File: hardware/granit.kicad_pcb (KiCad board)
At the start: 4 copper layers, 92 x 100 mm, 120 parts, among them IC1 ASM1061, J1 12V Barrel, J2 12V Screw Terminal, J3 RJ45_RB1-125B8G1A, J6 PCM12SMTR, J7 USB_C_Receptacle_USB2.0_14P, J8 BM03B-SRSS-TB, J9 SATA_22pin, Q1 FDS4435BZ, Q2 FDS4435BZ, Q3 FDS4435BZ, Q4 2N7002, Q5 2N7002, Q6 2N7002, SW1 SW_Push, U1 NCP1117-3.3_SOT223, U2 AP64501SP-13, U3 74AHCT1G125, U4 DS3231MZ, U5 USBLC6-2SC6, U6 74AHCT1G32, Y1 25MHz

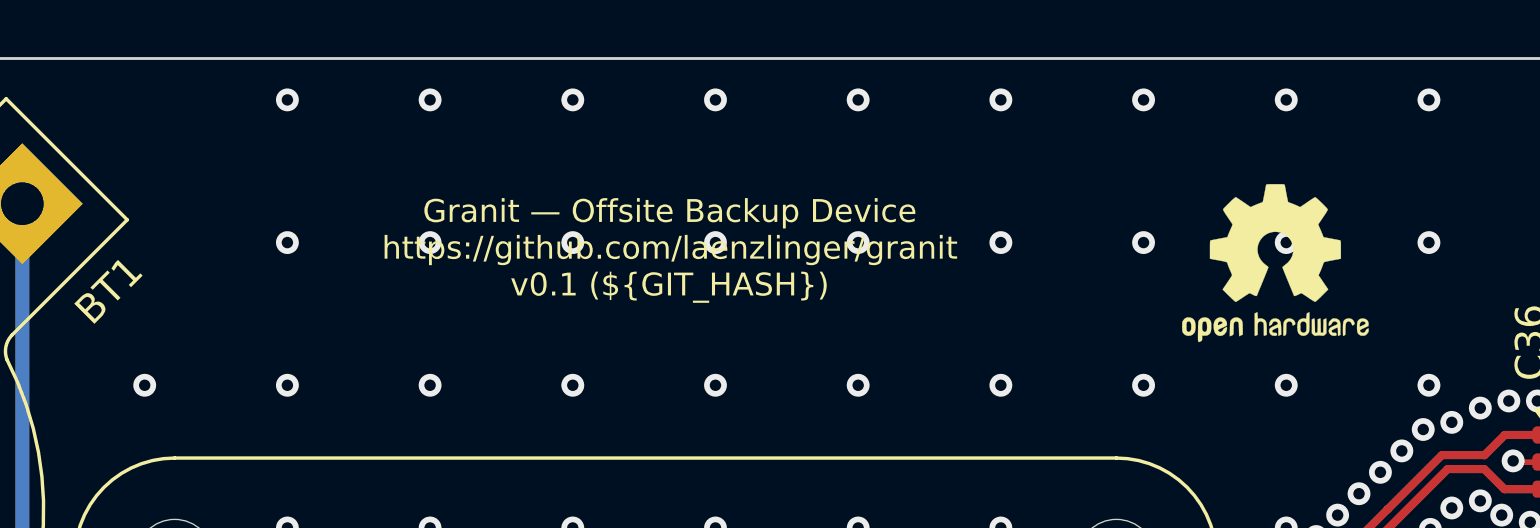
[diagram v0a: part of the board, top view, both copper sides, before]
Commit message: feat: add QR code linking to GitHub repo on front silkscreen
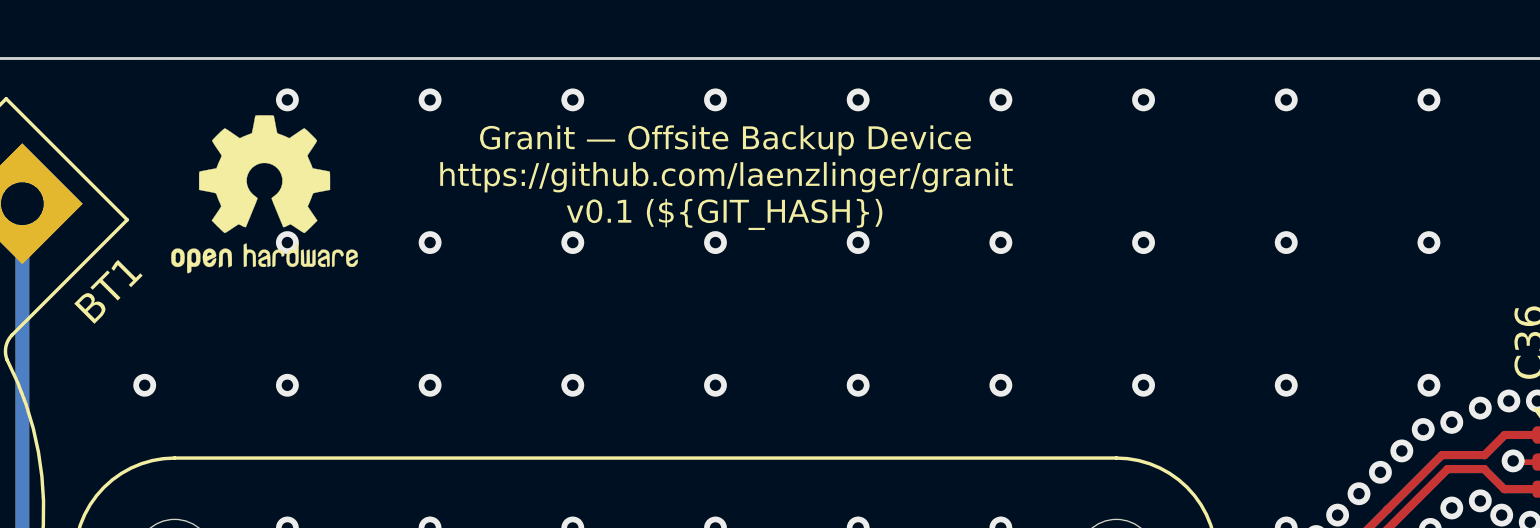
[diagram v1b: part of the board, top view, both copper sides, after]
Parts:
- moved SYM1 35.5 mm to (55.6, 24.8)
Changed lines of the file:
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@@
 	(footprint "Symbol:OSHW-Logo2_7.3x6mm_SilkScreen"
 		(layer "F.Cu")
-		(at 91.070714 27.162714)
+		(at 55.65 24.75)
 		(descr "Open Source Hardware Symbol")
 		(tags "Logo Symbol OSHW")
@@
 	)
 	(gr_text "${TITLE}\n${COMPANY}\nv${REVISION} (${GIT_HASH})"
-		(at 69.85 28.4 0)
+		(at 71.8 25.85 0)
 		(layer "F.SilkS")
 		(effects
@@
 		)
 	)
+	(barcode
+		(at 90.75 26.3 0)
+		(layer "F.SilkS")
+		(size 10 10)
+		(text " https://github.com/laenzlinger/granit")
+		(text_height 1)
+		(type qr)
+		(ecc_level M)
+		(hide yes)
+		(knockout no)
+	)
 	(segment

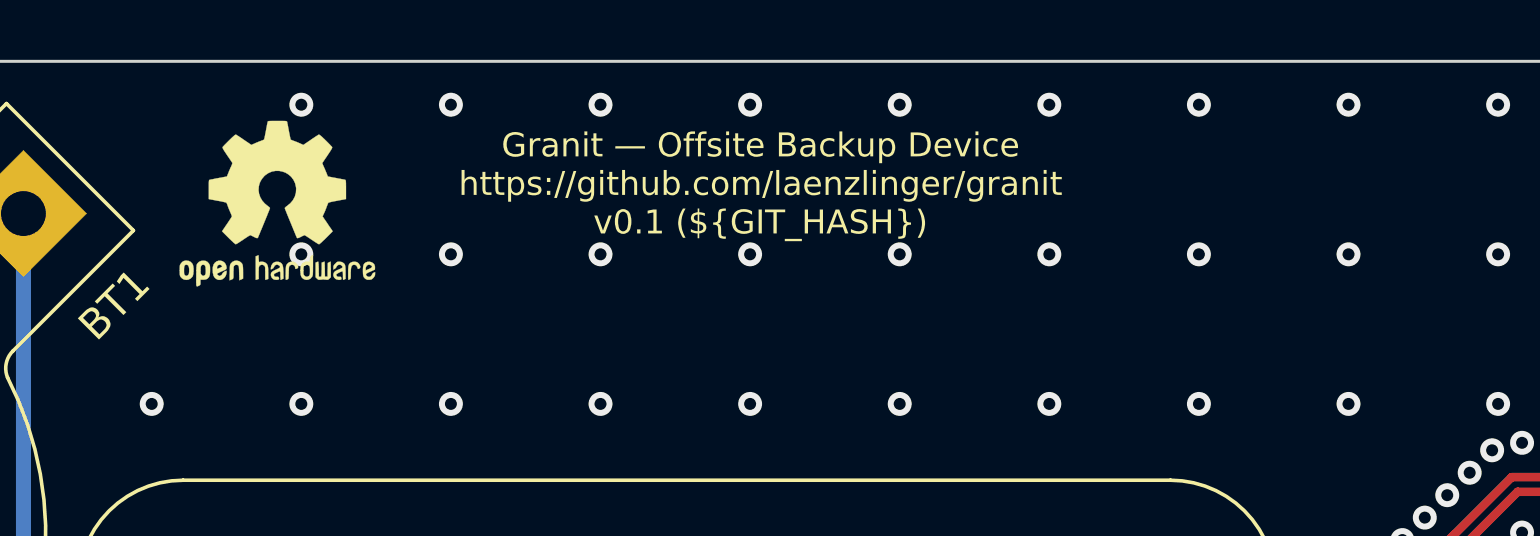
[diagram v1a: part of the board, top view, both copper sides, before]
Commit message: fix: DRC clean — mirror back silkscreen, clear QR code area, re-enable DRC in kibot
ERC: 0 errors, 0 warnings
DRC: 0 violations, 0 unconnected, 0 parity issues
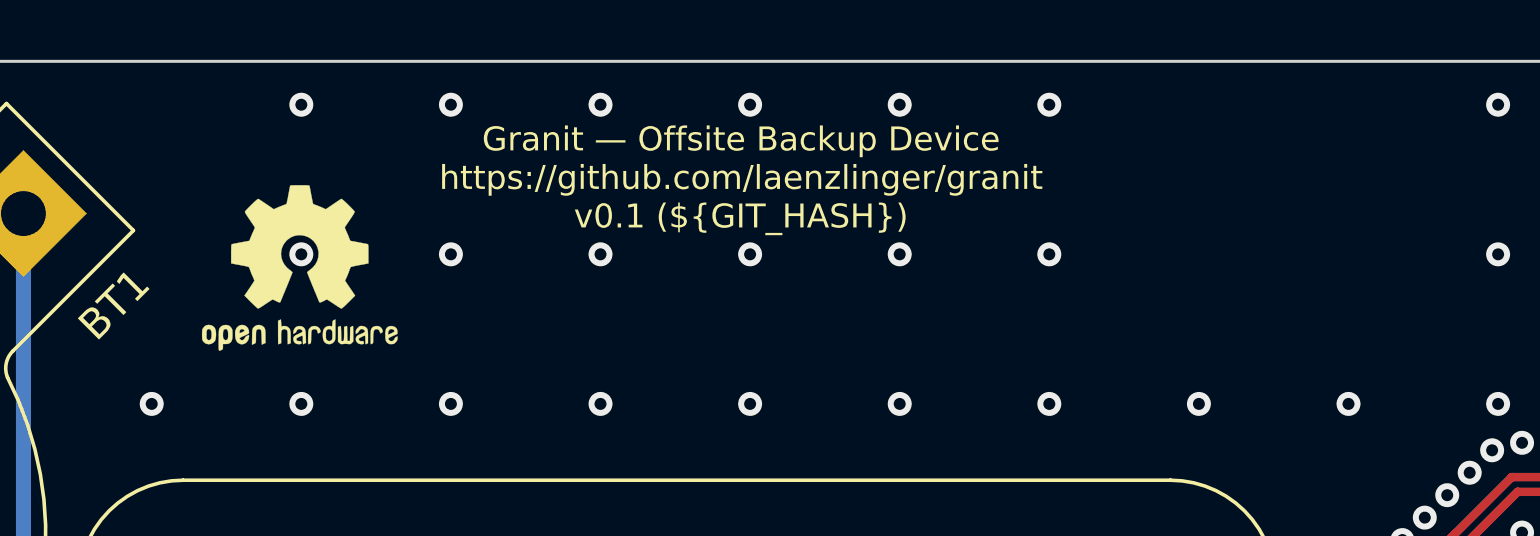
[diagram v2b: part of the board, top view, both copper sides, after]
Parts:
- moved SYM1 2.28 mm to (56.4, 26.9)
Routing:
- net GND: vias 454 -> 450
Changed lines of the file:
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@@
 	(footprint "Symbol:OSHW-Logo2_7.3x6mm_SilkScreen"
 		(layer "F.Cu")
-		(at 55.65 24.75)
+		(at 56.4 26.9)
 		(descr "Open Source Hardware Symbol")
 		(tags "Logo Symbol OSHW")
@@
 	)
 	(gr_text "${TITLE}\n${COMPANY}\nv${REVISION} (${GIT_HASH})"
-		(at 71.8 25.85 0)
+		(at 71.15 25.65 0)
 		(layer "F.SilkS")
 		(effects
@@
 				(thickness 0.15)
 			)
+			(justify mirror)
 		)
 	)
 	(barcode
-		(at 90.75 26.3 0)
+		(at 89.2 25.6 0)
 		(layer "F.SilkS")
-		(size 10 10)
+		(size 9 9)
 		(text " https://github.com/laenzlinger/granit")
 		(text_height 1)
@@
 	)
 	(via
-		(at 86.45 21.45)
-		(size 0.8)
-		(drill 0.4)
-		(layers "F.Cu" "B.Cu")
-		(net "GND")
-	)
-	(via
 		(at 96.5 81.75)
 		(size 0.8)
@@
 	)
 	(via
-		(at 91.45 21.45)
-		(size 0.8)
-		(drill 0.4)
-		(layers "F.Cu" "B.Cu")
-		(net "GND")
-	)
-	(via
 		(at 85.45 116.6)
 		(size 0.8)
@@
 	)
 	(via
-		(at 86.45 26.45)
-		(size 0.8)
-		(drill 0.4)
-		(layers "F.Cu" "B.Cu")
-		(net "GND")
-	)
-	(via
 		(at 44.8 57.25)
 		(size 0.8)
@@
 		(net "GND")
 	)
-	(via
-		(at 91.45 26.45)
-		(size 0.8)
-		(drill 0.4)
-		(layers "F.Cu" "B.Cu")
-		(net "GND")
-	)

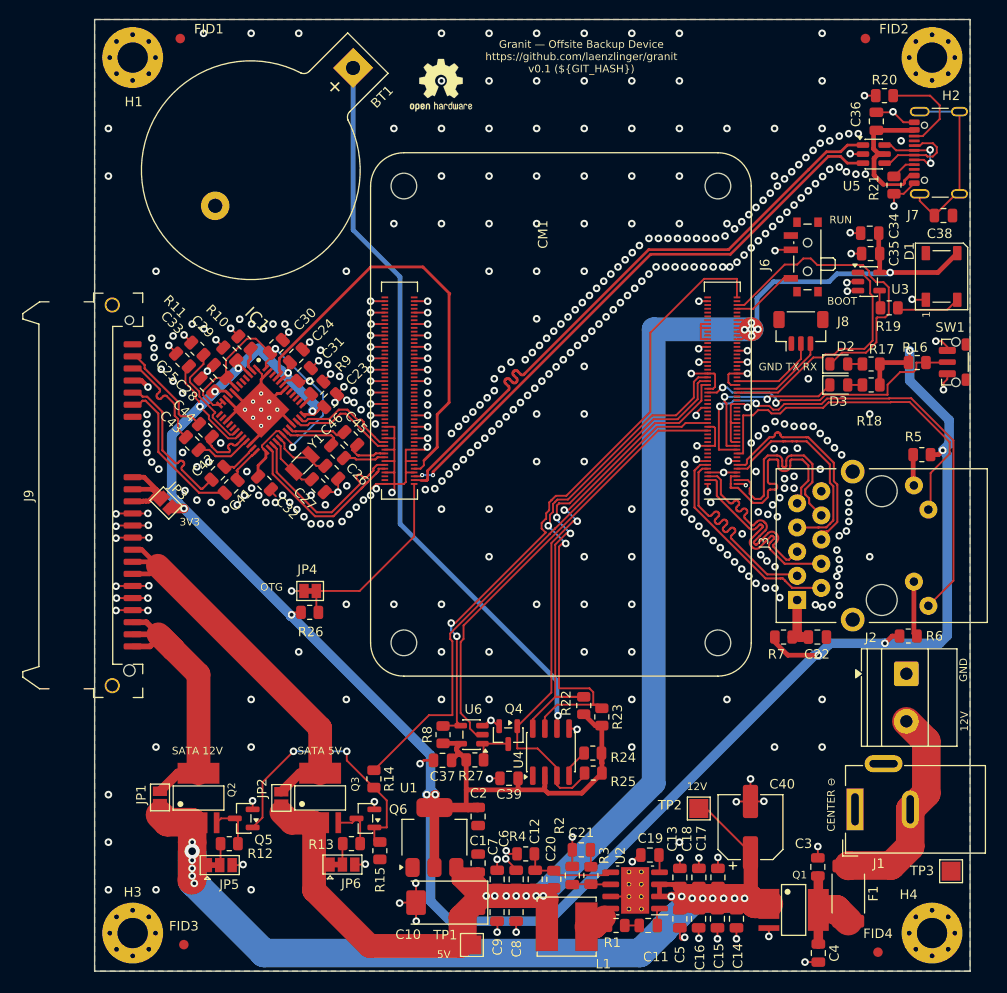
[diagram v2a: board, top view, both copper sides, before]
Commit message: refactor: reannotate PCB by position + rename IC1 to U prefix
All reference designators renumbered top-to-bottom, left-to-right.
ASM1061 changed from IC to U prefix.
ERC: 0 errors. DRC: 0 violations. Parity: 0 issues.
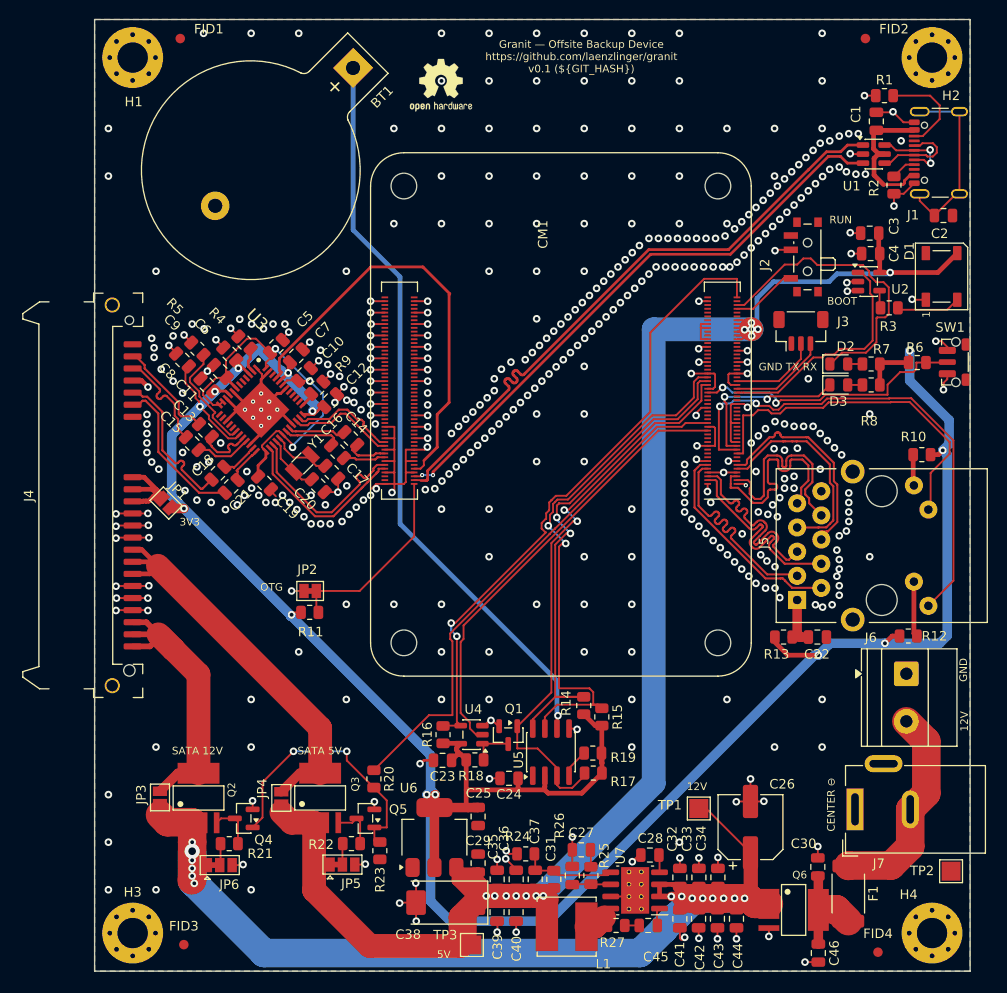
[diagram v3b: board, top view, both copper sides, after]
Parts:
- renumbered C36 to C1, C31 to C10, C28 to C11, C23 to C12, C44 to C13, C45 to C14, C43 to C15, C46 to C16, C26 to C17, C42 to C18, C32 to C19, C38 to C2, C27 to C20, C41 to C21, C37 to C23, C39 to C24, C2 to C25, C40 to C26, C21 to C27, C19 to C28, C1 to C29, C34 to C3, C3 to C30, C20 to C31, C13 to C32, C18 to C33, C17 to C34, C7 to C35, C6 to C36, C12 to C37, C10 to C38, C9 to C39, C35 to C4, C8 to C40, C5 to C41, C16 to C42, C15 to C43, C14 to C44, C11 to C45, C4 to C46, C30 to C5, C29 to C6, C24 to C7, C25 to C8, C33 to C9, J7 to J1, J6 to J2, J8 to J3, J9 to J4, J3 to J5, J2 to J6, J1 to J7, JP3 to JP1, JP4 to JP2, JP1 to JP3, JP2 to JP4, JP6 to JP5, JP5 to JP6, Q4 to Q1, Q5 to Q4, Q6 to Q5, Q1 to Q6, R20 to R1, R5 to R10, R26 to R11, R6 to R12, R7 to R13, R22 to R14, R23 to R15, R8 to R16, R25 to R17, R27 to R18, R24 to R19, R21 to R2, R14 to R20, R12 to R21, R13 to R22, R15 to R23, R4 to R24, R3 to R25, R2 to R26, R1 to R27, R19 to R3, R10 to R4, R11 to R5, R16 to R6, R17 to R7, R18 to R8, TP2 to TP1, TP3 to TP2, TP1 to TP3, U5 to U1, U3 to U2, IC1 to U3, U6 to U4, U4 to U5, U1 to U6, U2 to U7

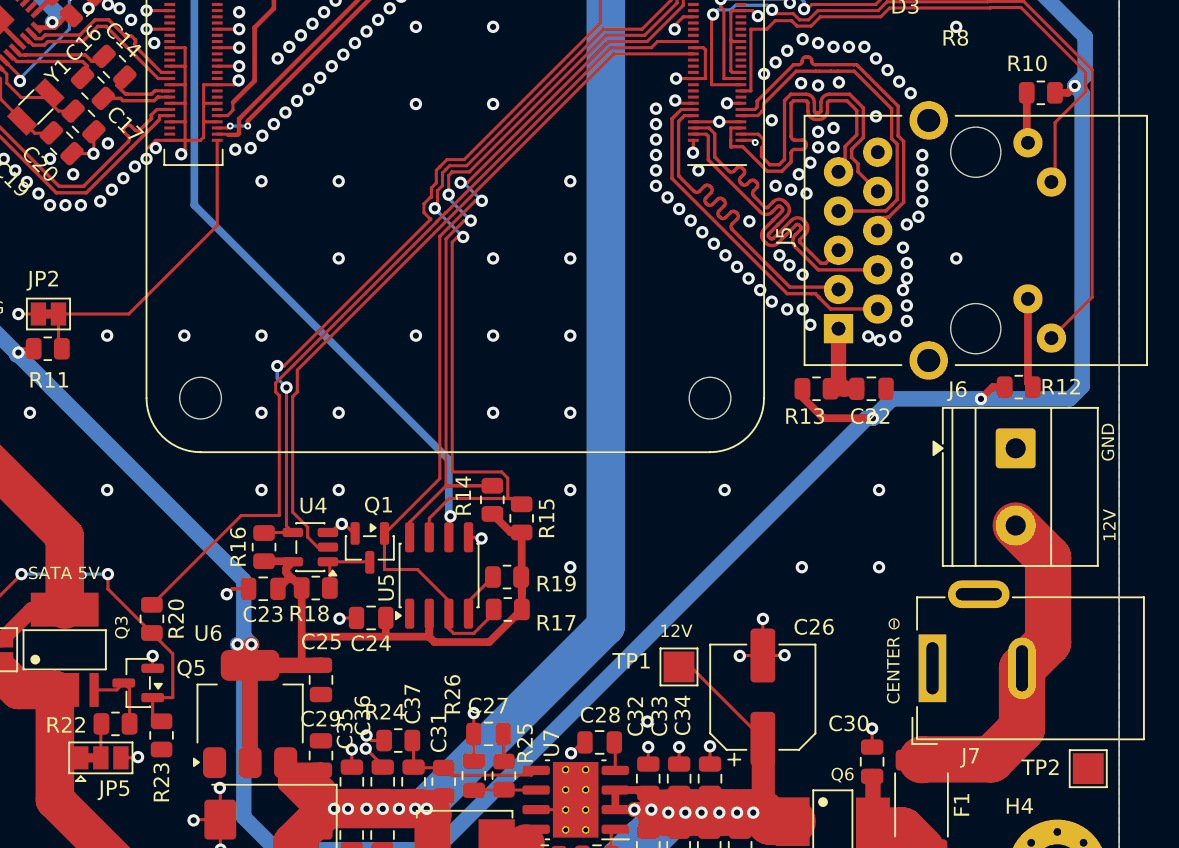
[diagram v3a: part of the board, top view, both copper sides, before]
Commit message: fix: sync PCB net names after reannotation
DRC: 0 violations, 0 parity issues.
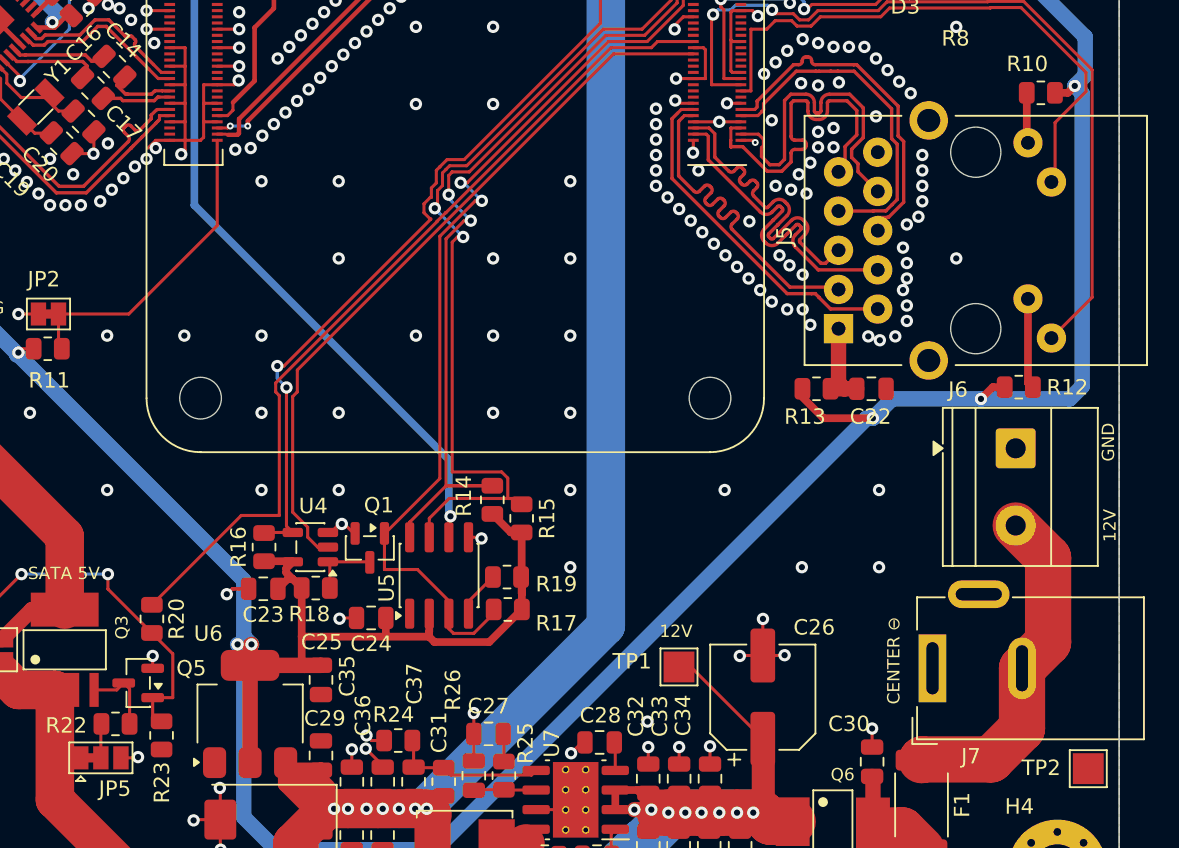
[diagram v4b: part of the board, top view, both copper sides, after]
